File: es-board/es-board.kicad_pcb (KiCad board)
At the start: 2 copper layers, 81.4 x 42.1 mm, 54 parts, among them J1 Conn_02x02_Odd_Even, J3 USB_C_Receptacle_USB2.0, Q1 Q_PMOS_GSD, Q2 Q_PMOS_GSD, Q3 Q_PMOS_GSD, Q4 Q_PMOS_GSD, Q5 NMOS, SW1 SW_SPST, SW2 SW_SPST, SW3 SW_SPST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

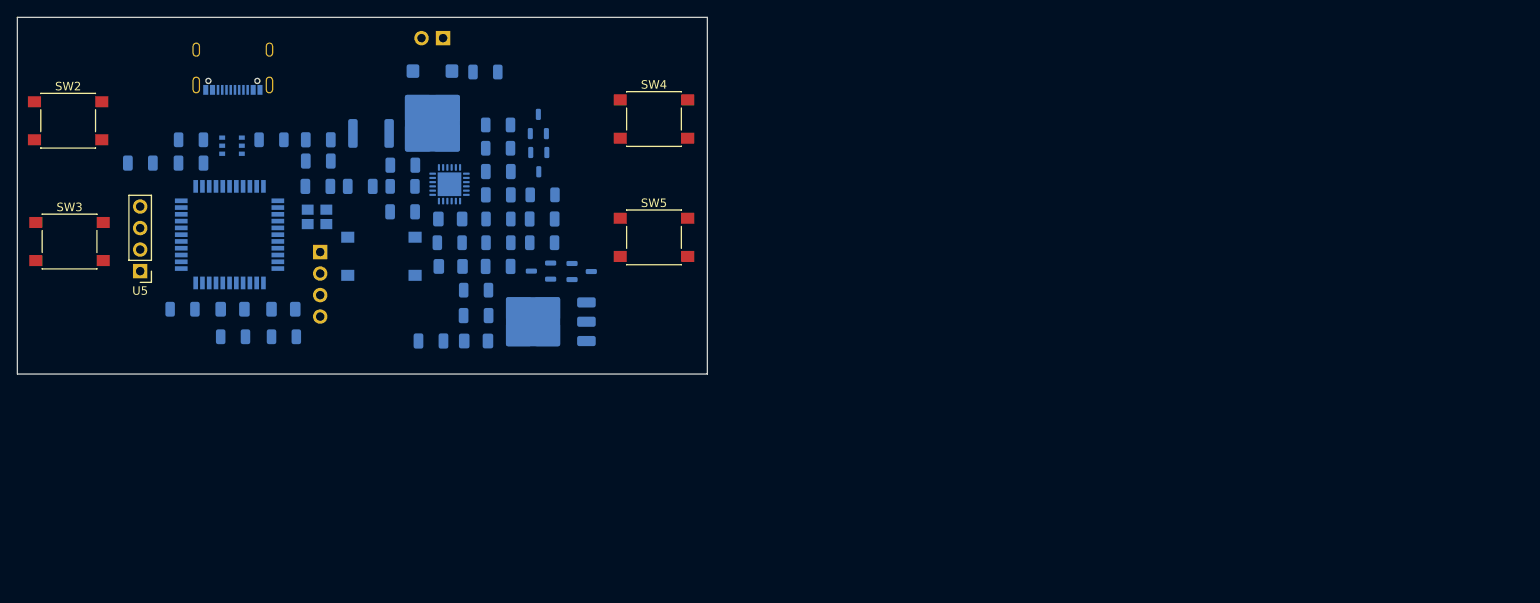
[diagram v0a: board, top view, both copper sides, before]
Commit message: Created pdfs of schematic and board layout
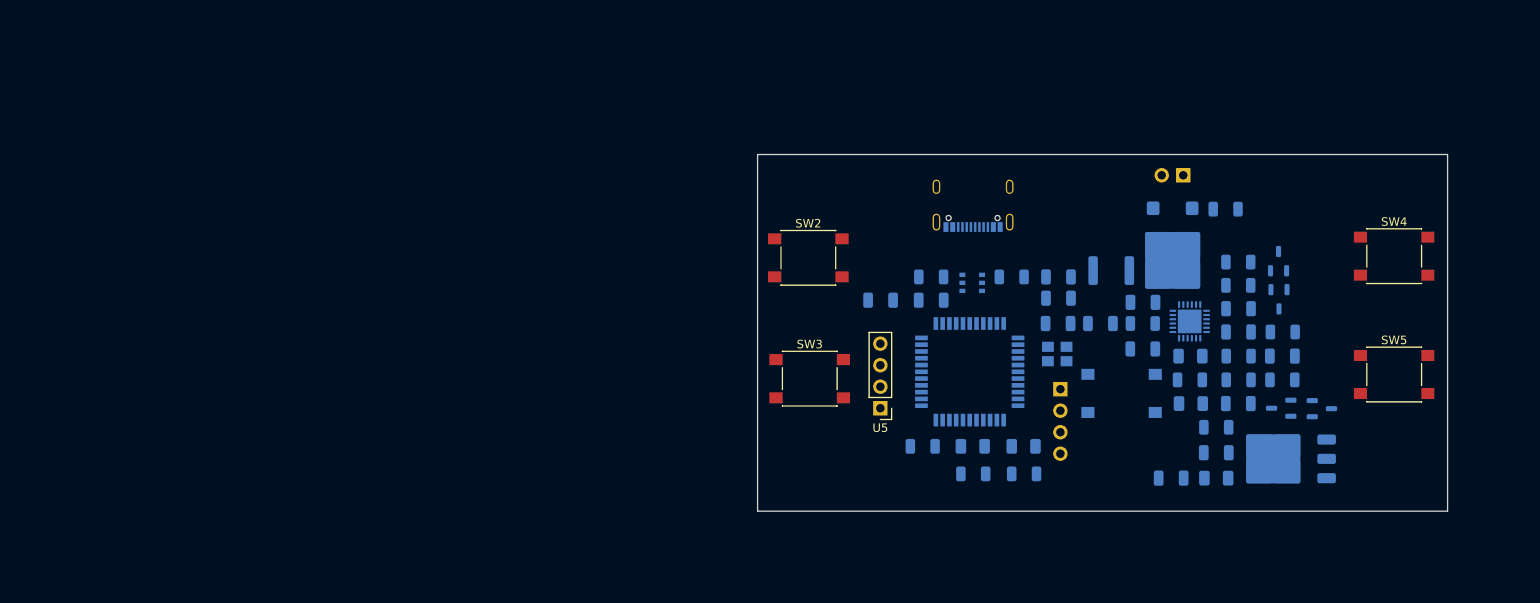
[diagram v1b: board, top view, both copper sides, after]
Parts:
- moved C1 88.9 mm to (151.1, 89.9)
- moved C10 88.9 mm to (162.4, 96.4)
- moved C15 88.9 mm to (155.9, 69.4)
- moved C2 88.9 mm to (146.1, 86.9)
- moved C3 88.9 mm to (141.1, 86.9)
- moved C4 88.9 mm to (120.1, 84.2)
- moved C8 88.9 mm to (151.1, 84.4)
- moved D4 88.9 mm to (156.7, 90.8)
- moved F1 88.9 mm to (147.4, 80.7)
- moved J1 88.9 mm to (141.4, 94.7)
- moved J3 88.9 mm to (131.1, 73.0)
- moved Q1 88.9 mm to (167.4, 96.9)
- moved Q3 88.9 mm to (167.1, 79.6)
- moved Q5 88.9 mm to (154.6, 78.3)
- moved R1 88.9 mm to (151.1, 86.9)
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
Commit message: Did some routing
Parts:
- moved C13 39.2 mm to (170.7, 69.5), turned to -90 degrees
- moved R4 29.7 mm to (139.8, 77.2), turned to 180 degrees
- moved D3 27.5 mm to (139.8, 74.7)
- moved C10 27.4 mm to (167.6, 69.5), turned to -90 degrees
- moved R13 25.4 mm to (164.5, 69.5), turned to -90 degrees
- moved U4 24.3 mm to (165.6, 78.7)
- moved C11 23.4 mm to (145.6, 71.6), turned to 0 degrees
- moved U1 23.3 mm to (140.1, 70.3), turned to 90 degrees
- moved D4 21.9 mm to (161.7, 69.5), turned to -90 degrees
- moved R12 21.7 mm to (145.6, 77.1)
- moved R11 19.9 mm to (145.6, 68.9)
- moved R10 18.6 mm to (145.6, 74.4)
- moved Q4 14.5 mm to (156.5, 93.9), turned to 90 degrees
- moved Q3 13.5 mm to (156.6, 88.0)
- moved C2 8.39 mm to (145.2, 95.3), turned to 90 degrees
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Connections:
- SW2 pad 1: io8 - UP -> io8
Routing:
- net GND: track 0.00 -> 196.6 mm, vias 0 -> 7
- net +5V: track 0.00 -> 63.5 mm, vias 0 -> 2
- net VBUS: track 0.00 -> 51.4 mm, vias 0 -> 2
- net io8: track 0.00 -> 40.1 mm, vias 0 -> 1
- net io10: track 0.00 -> 27.8 mm, vias 0 -> 1
- net a1: track 0.00 -> 19.9 mm
- net Net-(Q1-D): track 0.00 -> 16.4 mm
- net USB_CC1: track 0.00 -> 15.8 mm
- net Net-(Q3-G): track 0.00 -> 15.2 mm
- net VBUS_RAW: track 0.00 -> 14.9 mm
- net /Power/3v3_usbpd: track 0.00 -> 14.6 mm
- net d3/scl: track 0.00 -> 14.6 mm
- net USB_D-: track 0.00 -> 13.3 mm, vias 0 -> 2
- net USB_CC2: track 0.00 -> 13.3 mm
- net Net-(D5-A): track 0.00 -> 11.4 mm
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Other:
- board size 81.4 x 42.1 mm -> 82.5 x 48.2 mm

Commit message: Added BOM
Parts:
- C10, C8: value 10u -> 10u 50V
- C2, C3: value 18p -> 24p
- C9: value 1u -> 1u 50V
- D3: value LED -> red
- D4: value LED -> green
- J1: value Conn_02x02_Odd_Even -> DNP
- Q5: value NMOS -> IRF530NSTRLPB; footprint Package_TO_SOT_SMD:ATPAK-2 -> explosnake:TO-263-2_TabPin2
- R11: value 50k -> 51k
- SW1, SW2, SW3, SW4, SW5: footprint Button_Switch_SMD:SW_Push_1P1T_NO_6x6mm_H9.5mm -> Button_Switch_SMD:SW_SPST_SKQG_WithStem
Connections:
- Q5 pad 1: Net-(Q5-D) -> io9
- Q5 pad 2: io9 -> Net-(Q5-D)
- SW2 pad 1: io8 -> io8 - UP

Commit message: Updated board layout
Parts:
- moved D5 33.5 mm to (177.0, 76.5), turned to 0 degrees
- moved R17 33.1 mm to (134.7, 75.5)
- moved C14 28.7 mm to (177.0, 79.2), turned to 0 degrees
- moved R3 26.7 mm to (144.3, 74.9), turned to 0 degrees
- moved C9 24.9 mm to (150.1, 73.0)
- moved R2 24.2 mm to (154.8, 73.0)
- moved Q1 23.9 mm to (155.1, 76.5), turned to 0 degrees
- moved Q2 23.8 mm to (160.3, 76.5)
- moved R14 21.3 mm to (182.2, 73.4), turned to 180 degrees
- moved Q5 14.1 mm to (165.9, 86.8), turned to 180 degrees
- moved C10 14.0 mm to (181.6, 69.3)
- moved D4 14.0 mm to (175.7, 69.3)
- moved R13 14.0 mm to (178.5, 69.3)
- moved C12 14.0 mm to (145.9, 77.7)
- moved D3 11.0 mm to (128.8, 74.8), turned to 0 degrees
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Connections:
- SW2 pad 1: io8 - UP -> io8
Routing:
- net GND: track 196.6 -> 283.7 mm, vias 7 -> 12
- net io9: track 7.79 -> 93.7 mm, vias 0 -> 2
- net io12: track 0.00 -> 61.4 mm, vias 0 -> 1
- net io11: track 0.00 -> 51.7 mm, vias 0 -> 1
- net +5V: track 63.5 -> 105.0 mm, vias 2 -> 3
- net Net-(Q1-D): track 16.4 -> 56.3 mm, vias 0 -> 2
- net Net-(Q3-G): track 15.2 -> 50.2 mm
- net Net-(Q1-G): track 0.00 -> 19.7 mm
- net VBUS: track 51.4 -> 68.5 mm
- net Net-(Q5-D): track 4.31 -> 15.1 mm
- net Net-(U3-DD+): track 0.00 -> 8.75 mm
- net VBUS_RAW: track 14.9 -> 23.6 mm
- net Net-(U3-HD-): track 8.05 -> 14.9 mm
- net Net-(U3-HD+): track 8.15 -> 14.8 mm
- net Net-(U2-XTAL2): track 3.71 -> 9.16 mm
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
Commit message: Finished electricaling
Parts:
- removed C15: value to boom, Connector_PinHeader_2.54mm:PinHeader_1x02_P2.54mm_Vertical
- added J2: Conn_01x04, Connector_PinHeader_2.54mm:PinHeader_1x04_P2.54mm_Vertical, F.Cu at (170.5, 96.3)
- added R15: 0, Resistor_SMD:R_1206_3216Metric, B.Cu at (143.4, 101.2)
- added R16: 0, Resistor_SMD:R_1206_3216Metric, B.Cu at (145.8, 101.2)
- added TP1: TestPoint, Connector_PinHeader_1.00mm:PinHeader_1x01_P1.00mm_Vertical, B.Cu at (130.8, 86.8)
- added TP2: TestPoint, Connector_PinHeader_1.00mm:PinHeader_1x01_P1.00mm_Vertical, B.Cu at (137.2, 99.5)
- added TP3: Conn_01x02, Connector_PinHeader_2.54mm:PinHeader_1x02_P2.54mm_Vertical, B.Cu at (140.3, 95.3)
- J1: footprint Connector_PinHeader_2.54mm:PinHeader_1x04_P2.54mm_Vertical -> Connector_PinHeader_2.54mm:PinHeader_2x03_P2.54mm_Vertical
- SW1, SW2, SW3, SW4, SW5: footprint Button_Switch_SMD:SW_SPST_SKQG_WithStem -> explosnake:SW_SPST_SKQG_WithStem
- U5: moved to B.Cu
- moved U5 19.9 mm to (138.2, 105.5), turned to -90 degrees
- moved J1 17.6 mm to (134.0, 86.1)
- moved R14 12.9 mm to (178.4, 85.7), turned to 90 degrees
- moved R9 9.91 mm to (126.0, 83.4), turned to 90 degrees
- moved D2 9.28 mm to (125.5, 105.1)
- moved C4 8.08 mm to (119.1, 92.2)
- moved D3 7.27 mm to (134.7, 70.5)
- moved R4 7.27 mm to (134.7, 73.0)
- moved C10 5.90 mm to (175.7, 69.3)
- moved C7 5.30 mm to (130.8, 83.4), turned to 90 degrees
- moved U3 4.36 mm to (127.2, 79.2), turned to 180 degrees
- moved R6 4.36 mm to (123.1, 105.1)
- moved R7 3.41 mm to (127.8, 105.1)
- moved R13 2.80 mm to (181.3, 69.3), turned to 90 degrees
- moved D4 2.80 mm to (178.5, 69.3), turned to 90 degrees
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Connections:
- net Net-(Q1-D) renamed /Power/vbus_fused
- C13 pad 1: VBUS -> GND
- C14 pad 2: VBUS -> GND
- J1 pad 1: d1/tx -> miso
- J1 pad 2: d3/scl -> +5V
- J1 pad 3: d0/rx -> sck
- J1 pad 4: d2/sda -> mosi
- Q5 pad 1: io9 -> capboom
- R14 pad 2: io9 -> capboom
- SW2 pad 1: io8 -> btnUP
- SW3 pad 1: io10 - DOWN -> btnDOWN
- SW4 pad 1: io11 - LEFT -> btnLEFT
- SW5 pad 1: io12 - RIGHT -> btnRIGHT
- U2 pad 1: d7 -> unconnected-(U2-PE6-Pad1)
- U2 pad 12: io11 -> USB_PD_FAULT
- U2 pad 18: d3/scl -> Net-(U2-PD0)
- U2 pad 19: d2/sda -> Net-(U2-PD1)
- U2 pad 20: d0/rx -> /Digital/rx
- U2 pad 21: d1/tx -> /Digital/tx
- U2 pad 25: d4 -> unconnected-(U2-PD4-Pad25)
- U2 pad 26: io12 -> btnRIGHT
- U2 pad 27: d6 -> btnLEFT
- U2 pad 28: io8 -> capboom
- U2 pad 29: io9 -> btnUP
- U2 pad 30: io10 -> btnDOWN
- U2 pad 31: d5 -> unconnected-(U2-PC6-Pad31)
- U2 pad 36: a0 -> unconnected-(U2-PF7-Pad36)
- U2 pad 37: a1 -> unconnected-(U2-PF6-Pad37)
- U2 pad 38: a2 -> unconnected-(U2-PF5-Pad38)
- U2 pad 39: a3 -> unconnected-(U2-PF4-Pad39)
- U2 pad 40: a4 -> unconnected-(U2-PF1-Pad40)
- U2 pad 41: a5 -> unconnected-(U2-PF0-Pad41)
- U4 pad 2: VBUS -> GND
- U5 pad 3: a1 -> scl
- U5 pad 4: a0 -> sda
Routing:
- net GND: track 283.7 -> 38.3 mm, vias 12 -> 69
- net io9: track 93.7 -> 0.00 mm, vias 2 -> 0
- net capboom: track 0.00 -> 81.7 mm, vias 0 -> 2
- net btnLEFT: track 0.00 -> 81.0 mm, vias 0 -> 1
- net btnRIGHT: track 0.00 -> 65.2 mm, vias 0 -> 1
- net io12: track 61.4 -> 0.00 mm, vias 1 -> 0
- net io11: track 51.7 -> 0.00 mm, vias 1 -> 0
- net +5V: track 105.0 -> 153.2 mm, vias 3 -> 8
- net io8: track 42.5 -> 0.00 mm, vias 1 -> 0
- net btnUP: track 0.00 -> 39.1 mm, vias 0 -> 1
- net io10: track 29.6 -> 0.00 mm, vias 1 -> 0
- net Reset: track 9.53 -> 38.1 mm
- net btnDOWN: track 0.00 -> 22.6 mm, vias 0 -> 1
- net a1: track 22.0 -> 0.00 mm
- net Net-(U2-PD1): track 0.00 -> 15.6 mm, vias 0 -> 2
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- added copper zone on B.Cu, net GND
- added copper zone on F.Cu, net GND

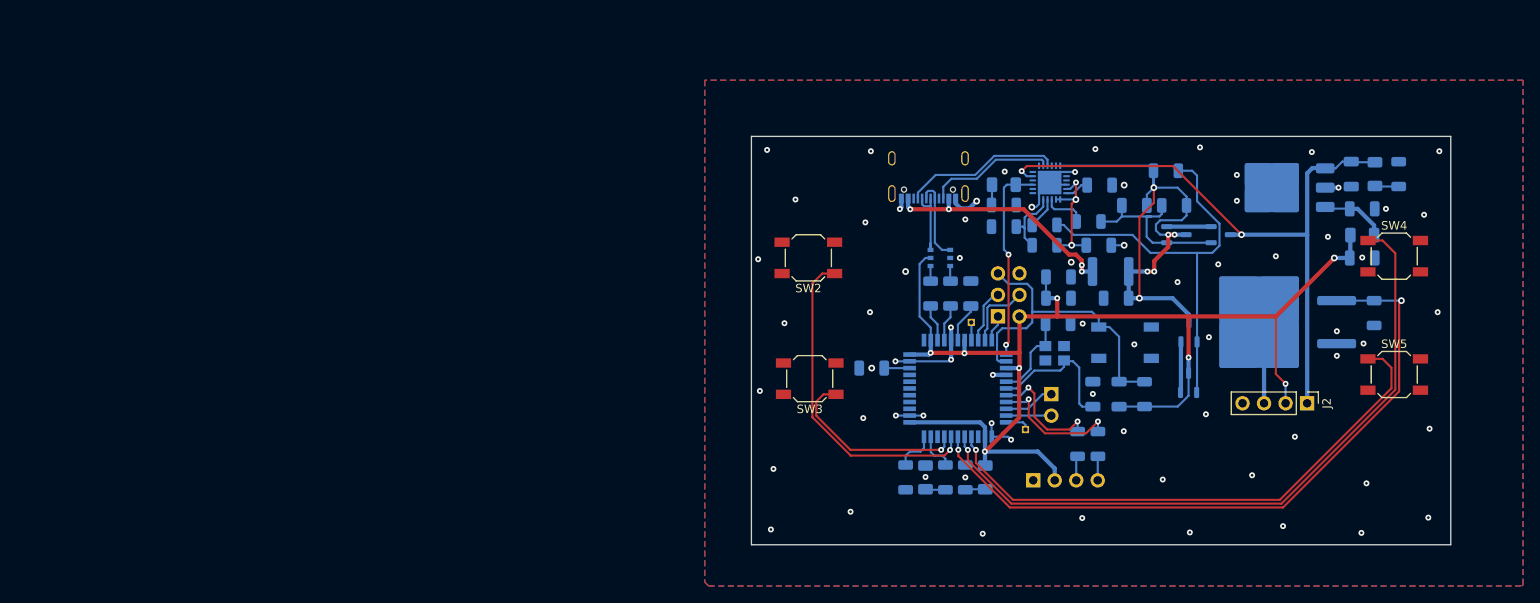
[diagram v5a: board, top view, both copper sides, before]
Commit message: Fixed board outline and silkscreen
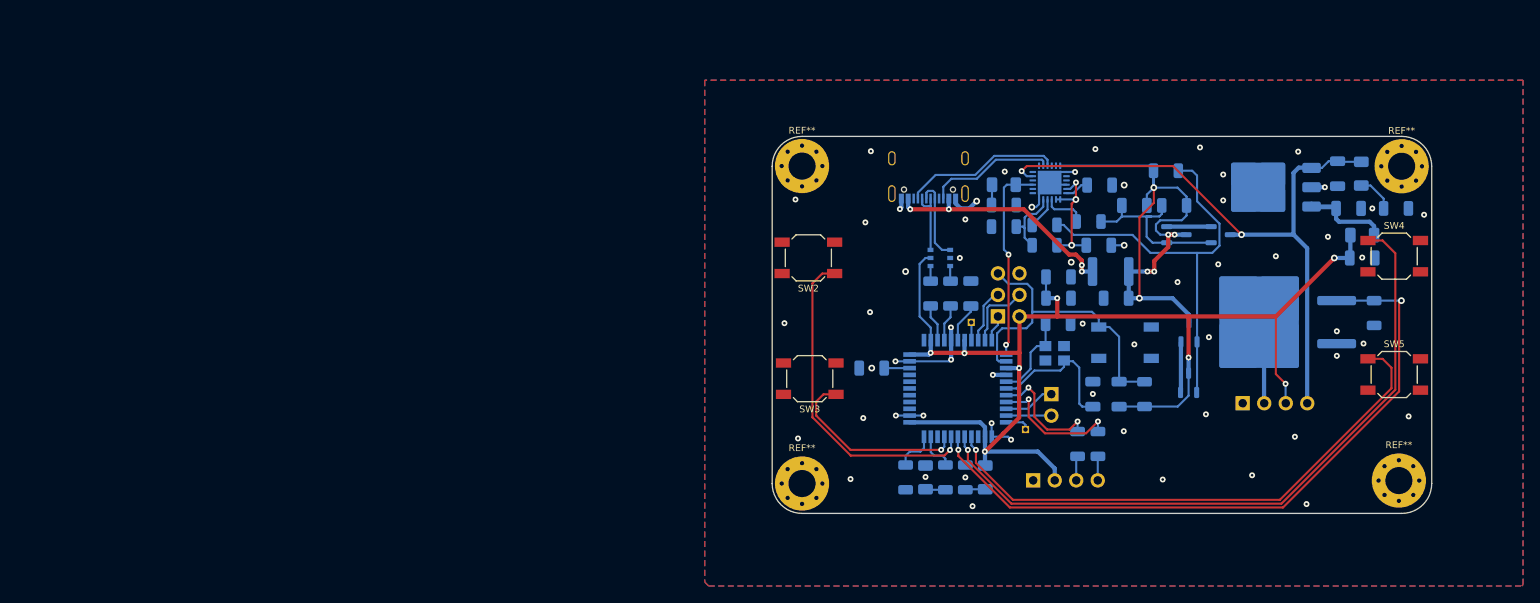
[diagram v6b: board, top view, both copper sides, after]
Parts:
- added REF**: MountingHole_3.2mm_M3_Pad_Via, MountingHole:MountingHole_3.2mm_M3_Pad_Via, F.Cu at (110.9, 68.3)
- added REF**: MountingHole_3.2mm_M3_Pad_Via, MountingHole:MountingHole_3.2mm_M3_Pad_Via, F.Cu at (181.3, 105.5)
- added REF**: MountingHole_3.2mm_M3_Pad_Via, MountingHole:MountingHole_3.2mm_M3_Pad_Via, F.Cu at (110.9, 105.8)
- added REF**: MountingHole_3.2mm_M3_Pad_Via, MountingHole:MountingHole_3.2mm_M3_Pad_Via, F.Cu at (181.7, 68.4)
- J2: moved to B.Cu
- moved J2 7.60 mm to (162.9, 96.3)
- moved R13 4.06 mm to (181.0, 73.3), turned to 0 degrees
- moved C13 1.61 mm to (175.4, 73.3)
- moved U4 1.61 mm to (166.0, 70.8)
- moved C10 1.61 mm to (174.1, 69.2)
- moved D4 1.61 mm to (176.9, 69.2)
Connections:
- J2 pad 1: VBUS -> GND
- J2 pad 2: +5V -> Net-(J2-Pin_2)
- J2 pad 3: Net-(J2-Pin_3) -> +5V
- J2 pad 4: GND -> VBUS
- Q5 pad 2: Net-(J2-Pin_3) -> Net-(J2-Pin_2)
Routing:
- net Net-(J2-Pin_3): track 10.8 -> 0.00 mm
- net Net-(J2-Pin_2): track 0.00 -> 10.8 mm
- net Net-(D5-A): track 8.02 -> 13.3 mm
- net Net-(D4-K): track 2.90 -> 4.59 mm
- net VBUS: track 76.1 -> 75.2 mm
- net Net-(U3-HD-): track 8.66 -> 7.85 mm
- net /Power/vbus_fused: track 69.3 -> 70.1 mm
- net GND: vias 69 -> 58
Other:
- board size 82.5 x 48.2 mm -> 77.9 x 44.5 mm
- board text added: "20v 5v t g"
- board text added: "5"
- board text added: "OLED"
- board text added: "c"
- board text added: "d c p g"
- board text added: "g"
- board text added: "i"
- board text added: "notifier"
- board text added: "o"
- board text added: "r"
- board text added: "rxled"
- board text added: "txled"

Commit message: Design review tweaks
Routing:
- net GND: vias 58 -> 60
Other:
- board text added: "${TITLE} ${COMPANY} ${CURRENT_DATE} ${REVISION}"
- board text added: "reset"
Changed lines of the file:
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@@
   (title_block
     (title "ExploSnake")
-    (date "2023-11-01")
-    (rev "v0.1")
+    (date "2023-11-15")
+    (rev "v1.0")
     (company "Team 2")
   )
@@
     (pad "1" thru_hole circle (at 0 -2.4) (size 0.8 0.8) (drill 0.5) (layers "*.Cu" "*.Mask")
       (net 4 "GND") (zone_connect 2))
-    (pad "1" thru_hole circle locked (at 0 0) (size 6.4 6.4) (drill 3.2) (layers "*.Cu" "*.Mask")
+    (pad "1" thru_hole circle (at 0 0) (size 6.4 6.4) (drill 3.2) (layers "*.Cu" "*.Mask")
       (net 4 "GND") (zone_connect 2))
     (pad "1" thru_hole circle (at 0 2.4) (size 0.8 0.8) (drill 0.5) (layers "*.Cu" "*.Mask")
@@
     (effects (font (size 1 1) (thickness 0.15)) (justify left bottom mirror))
   )
+  (gr_text "reset" (at 154.55 86.2) (layer "B.SilkS")
+    (effects (font (size 1 1) (thickness 0.15)) (justify left bottom mirror))
+  )
   (gr_text "rxled" (at 127.775 87.325) (layer "B.SilkS")
     (effects (font (size 1 1) (thickness 0.15)) (justify left bottom mirror))
@@
     (effects (font (size 1 1) (thickness 0.15)) (justify left bottom mirror))
   )
+  (gr_text "${TITLE}\n${COMPANY}\n${CURRENT_DATE} ${REVISION}" (at 151.05 106.15) (layer "F.SilkS")
+    (effects (font (size 1 1) (thickness 0.15)) (justify left bottom))
+  )
   (segment (start 136.54 92.16) (end 136.54 92.01) (width 0.5) (layer "F.Cu") (net 1))
   (segment (start 132.45 102.1) (end 132.5 102.05) (width 0.5) (layer "F.Cu") (net 1))
@@
   (via (at 178.188 73.35) (size 0.7) (drill 0.3) (layers "F.Cu" "B.Cu") (free) (net 4))
   (via (at 155.2 82.05) (size 0.7) (drill 0.3) (layers "F.Cu" "B.Cu") (free) (net 4))
+  (via (at 176.65 102.95) (size 0.8) (drill 0.4) (layers "F.Cu" "B.Cu") (free) (net 4))
   (via (at 118.9 85.6) (size 0.7) (drill 0.3) (layers "F.Cu" "B.Cu") (free) (net 4))
   (via (at 110.1 72.3) (size 0.7) (drill 0.3) (layers "F.Cu" "B.Cu") (free) (net 4))
@@
   (via (at 128.45 87.4) (size 0.7) (drill 0.3) (layers "F.Cu" "B.Cu") (free) (net 4))
   (via (at 169.05 100.3) (size 0.7) (drill 0.3) (layers "F.Cu" "B.Cu") (free) (net 4))
+  (via (at 174.75 96.1) (size 0.8) (drill 0.4) (layers "F.Cu" "B.Cu") (free) (net 4))
   (via (at 148.85 99.65) (size 0.7) (drill 0.3) (layers "F.Cu" "B.Cu") (free) (net 4))
   (via (at 121.9 91.4) (size 0.7) (drill 0.3) (layers "F.Cu" "B.Cu") (net 4))
